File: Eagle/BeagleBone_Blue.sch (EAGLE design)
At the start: 166 parts, among them M1 JST_ZH_2, M2 JST_ZH_2, M3 JST_ZH_2, M4 JST_ZH_2, Q3 MOSFET-N, U1 OSD3358, U2 CM200C-32.768KAZF-UT, U3 DMC564040R, U4 DMC564040R, U5 24LC_32AT-I/OT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

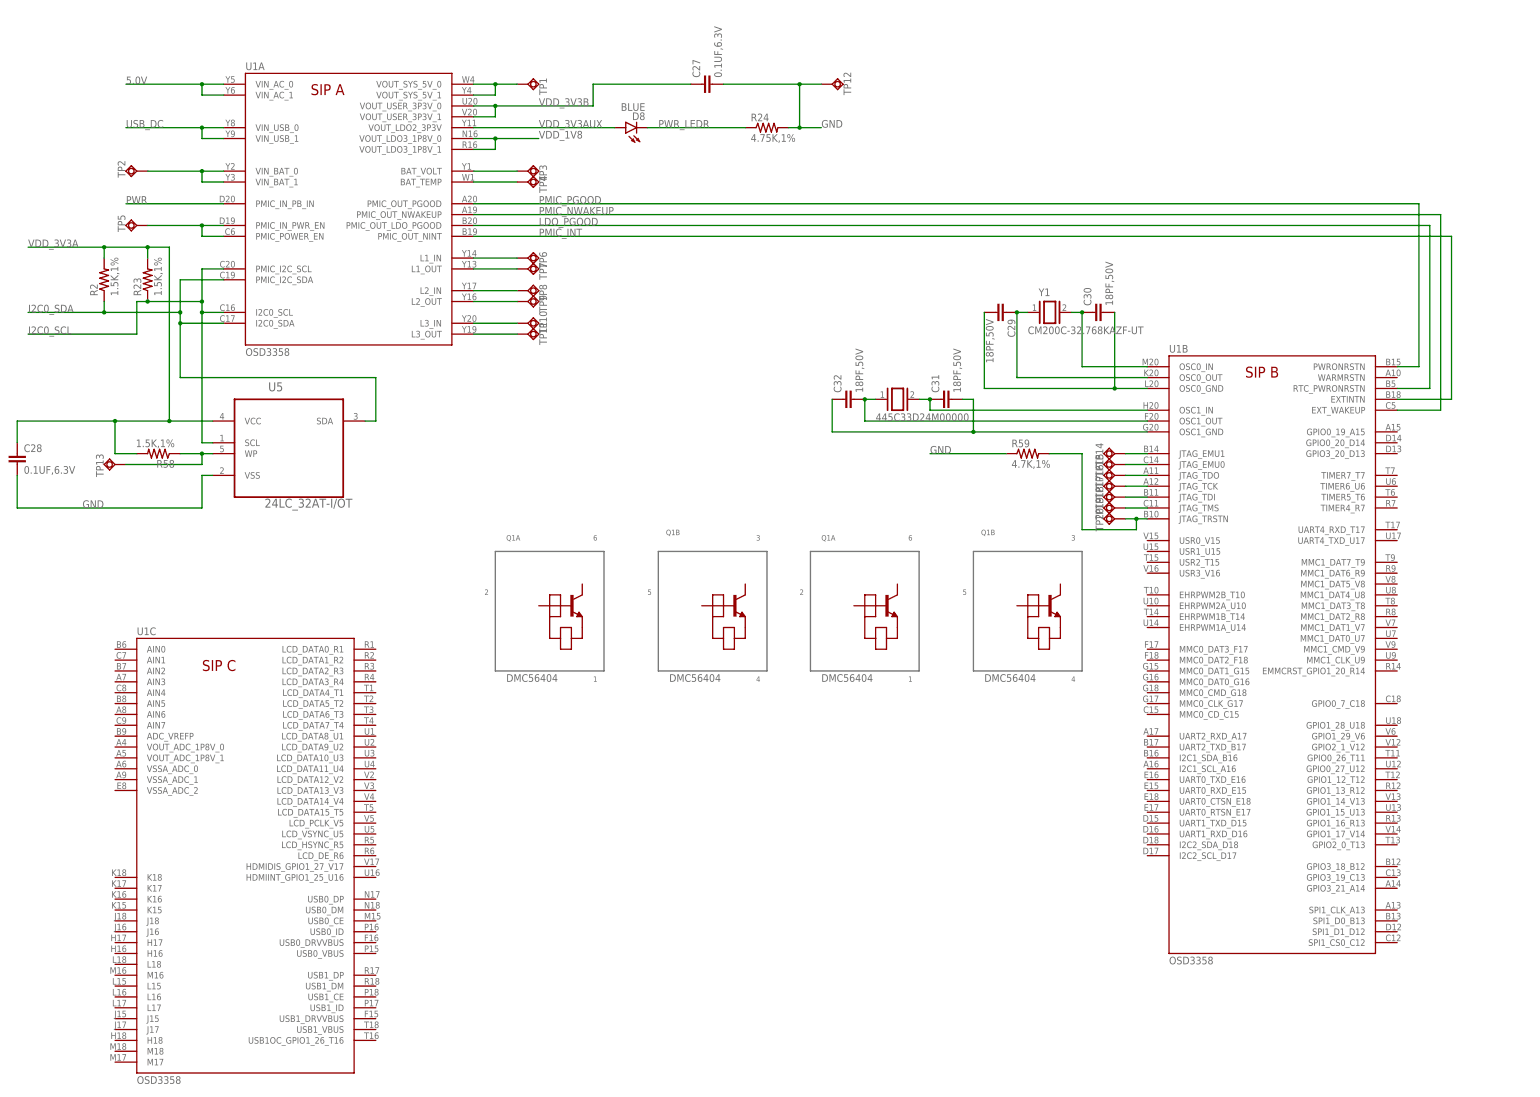
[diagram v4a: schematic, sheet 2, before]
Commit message: Added USRx LEDs
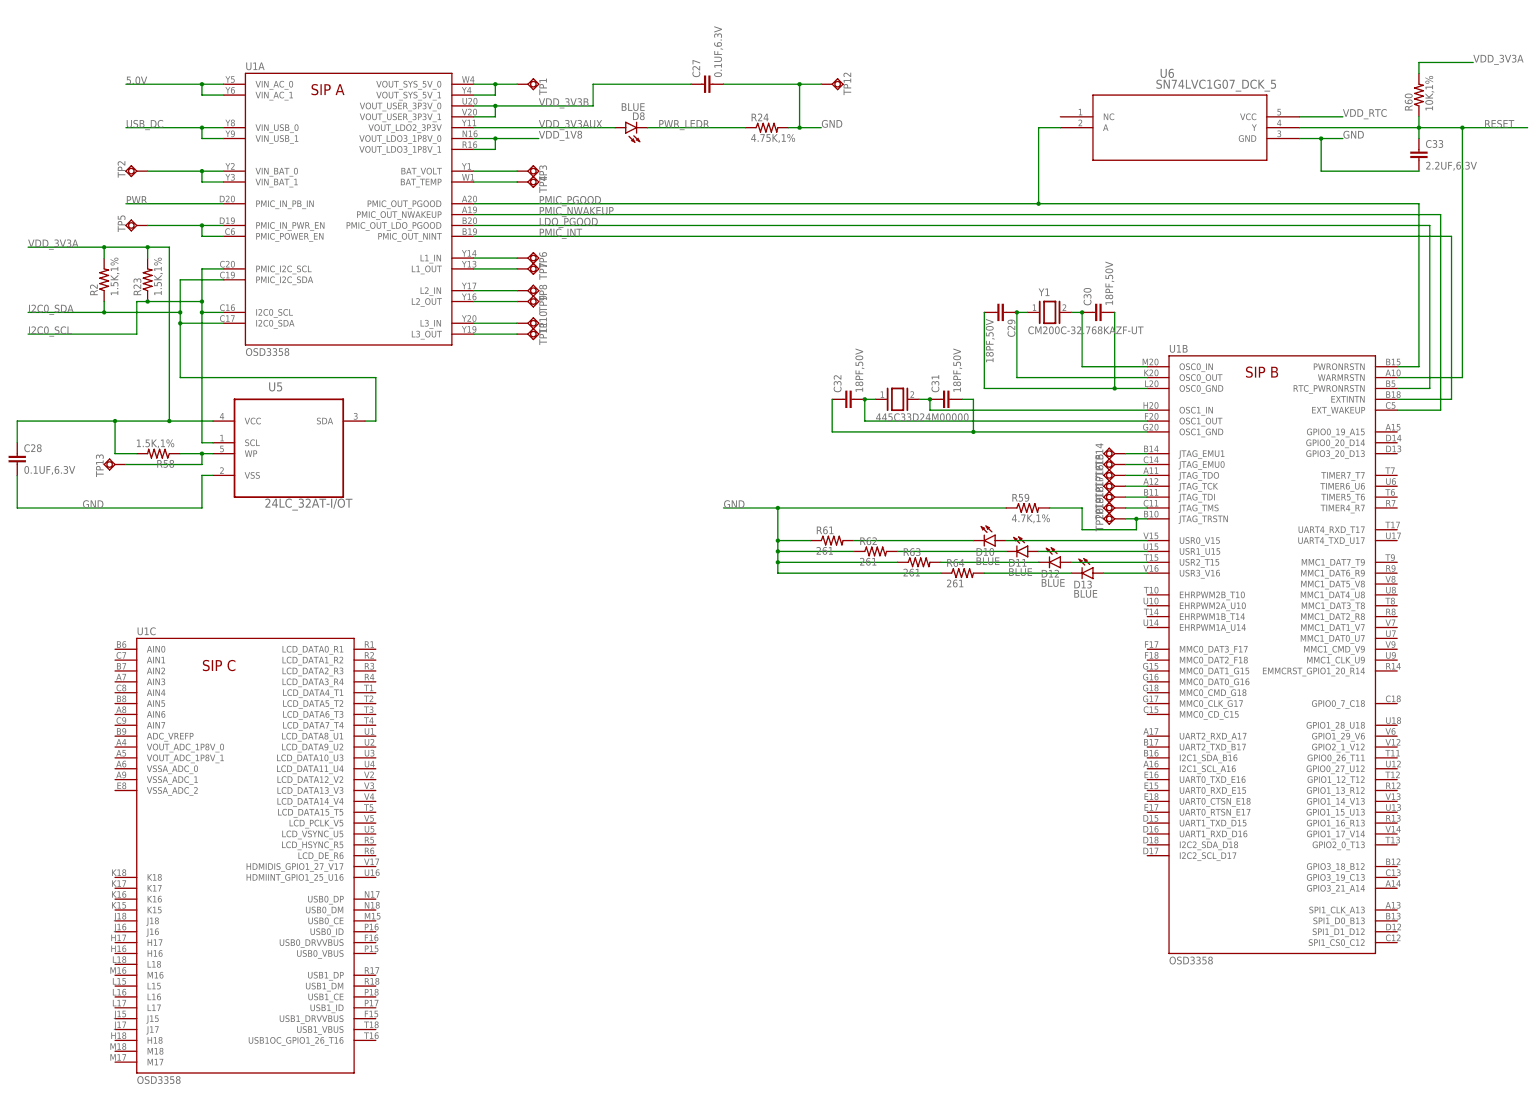
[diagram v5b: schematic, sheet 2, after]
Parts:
- removed U3, U4: DMC564040R, DMC564040R:DMC564040R
- added C33: 2.2UF,6.3V, Strawson_Eagle_Lib:CAP0402-CAP
- added D10, D11, D12, D13: BLUE, BeagleBone_Blue:LED0603
- added R60: 10K,1%, Strawson_Eagle_Lib:RESISTOR0402-RES
- added R61, R62, R63, R64: 261, Strawson_Eagle_Lib:RESISTOR0402-RES
- added U6: SN74LVC1G07_DCK_5, SN74LVC1G07:SN74LVC1G07_DCK_5
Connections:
- new net N$43: D13.A, U1B.USR3_V16
- new net N$44: D12.A, U1B.USR2_T15
- new net N$45: D11.A, U1B.USR1_U15
- new net N$46: D10.A, U1B.USR0_V15
- new net N$47: D10.C, R61.2
- new net N$57: D11.C, R62.2
- new net N$58: D12.C, R63.2
- new net N$59: D13.C, R64.2
- new net VDD_RTC: U6.VCC
- net GND: now also C33.2, R61.1, R62.1, R63.1, R64.1, U6.GND
- net PMIC_PGOOD: now also U6.A
- net RESET: now also C33.1, R60.1, U1B.WARMRSTN, U6.Y
- net VDD_3V3A: now also R60.2
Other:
- moved on the sheet: R59
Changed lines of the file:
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@@
 <part name="C27" library="Strawson_Eagle_Lib" deviceset="CAP" device="0402-CAP" value="0.1UF,6.3V"/>
 <part name="U2" library="CM200C-32.768KAZF-UT" deviceset="CM200C-32.768KAZF-UT" device=""/>
-<part name="U3" library="DMC564040R" deviceset="DMC564040R" device=""/>
-<part name="U4" library="DMC564040R" deviceset="DMC564040R" device=""/>
 <part name="U5" library="Microchip-24LCxxx" deviceset="24LC_" device="" technology="32AT-I/OT"/>
 <part name="R58" library="Strawson_Eagle_Lib" deviceset="RESISTOR" device="0402-RES" value="1.5K,1%"/>
@@
 <part name="TP20" library="testpad" deviceset="TPSQ" device="B1,27"/>
 <part name="R59" library="Strawson_Eagle_Lib" deviceset="RESISTOR" device="0402-RES" value="4.7K,1%"/>
+<part name="U6" library="SN74LVC1G07" deviceset="SN74LVC1G07_DCK_5" device=""/>
+<part name="C33" library="Strawson_Eagle_Lib" deviceset="CAP" device="0402-CAP" value="2.2UF,6.3V"/>
+<part name="R60" library="Strawson_Eagle_Lib" deviceset="RESISTOR" device="0402-RES" value="10K,1%"/>
+<part name="D10" library="BeagleBone_Blue" deviceset="LED" device="0603" value="BLUE"/>
+<part name="D11" library="BeagleBone_Blue" deviceset="LED" device="0603" value="BLUE"/>
+<part name="D12" library="BeagleBone_Blue" deviceset="LED" device="0603" value="BLUE"/>
+<part name="D13" library="BeagleBone_Blue" deviceset="LED" device="0603" value="BLUE"/>
+<part name="R61" library="Strawson_Eagle_Lib" deviceset="RESISTOR" device="0402-RES" value="261"/>
+<part name="R62" library="Strawson_Eagle_Lib" deviceset="RESISTOR" device="0402-RES" value="261"/>
+<part name="R63" library="Strawson_Eagle_Lib" deviceset="RESISTOR" device="0402-RES" value="261"/>
+<part name="R64" library="Strawson_Eagle_Lib" deviceset="RESISTOR" device="0402-RES" value="261"/>
 </parts>
 <sheets>
@@
 <instance part="C27" gate="G$1" x="180.34" y="248.92" rot="R90"/>
 <instance part="U2" gate="G$1" x="307.34" y="182.88"/>
-<instance part="U3" gate="G$1" x="238.76" y="121.92"/>
-<instance part="U4" gate="G$1" x="165.1" y="121.92"/>
 <instance part="U5" gate="A" x="63.5" y="170.18"/>
 <instance part="R58" gate="G$1" x="50.8" y="162.56" rot="R180"/>
@@
 <instance part="TP19" gate="G$1" x="274.32" y="149.86" rot="R270"/>
 <instance part="TP20" gate="G$1" x="274.32" y="147.32" rot="R270"/>
-<instance part="R59" gate="G$1" x="254" y="162.56"/>
+<instance part="R59" gate="G$1" x="254" y="149.86"/>
+<instance part="U6" gate="A" x="261.62" y="241.3"/>
+<instance part="C33" gate="G$1" x="345.44" y="231.14"/>
+<instance part="R60" gate="G$1" x="345.44" y="246.38" rot="R90"/>
+<instance part="D10" gate="G$1" x="246.38" y="142.24" rot="R270"/>
+<instance part="D11" gate="G$1" x="254" y="139.7" rot="R270"/>
+<instance part="D12" gate="G$1" x="261.62" y="137.16" rot="R270"/>
+<instance part="D13" gate="G$1" x="269.24" y="134.62" rot="R270"/>
+<instance part="R61" gate="G$1" x="208.28" y="142.24"/>
+<instance part="R62" gate="G$1" x="218.44" y="139.7"/>
+<instance part="R63" gate="G$1" x="228.6" y="137.16"/>
+<instance part="R64" gate="G$1" x="238.76" y="134.62"/>
 </instances>
 <busses>
@@
 <junction x="40.64" y="170.18"/>
 </segment>
+<segment>
+<pinref part="R60" gate="G$1" pin="2"/>
+<wire x1="345.44" y1="251.46" x2="345.44" y2="254" width="0.1524" layer="91"/>
+<wire x1="345.44" y1="254" x2="358.14" y2="254" width="0.1524" layer="91"/>
+<label x="358.14" y="254" size="1.778" layer="95"/>
+</segment>
 </net>
 <net name="VDD_3V3B" class="0">
@@
 <segment>
 <pinref part="R59" gate="G$1" pin="1"/>
-<wire x1="248.92" y1="162.56" x2="231.14" y2="162.56" width="0.1524" layer="91"/>
-<label x="231.14" y="162.56" size="1.778" layer="95"/>
+<wire x1="248.92" y1="149.86" x2="195.58" y2="149.86" width="0.1524" layer="91"/>
+<label x="182.88" y="149.86" size="1.778" layer="95"/>
+<pinref part="R64" gate="G$1" pin="1"/>
+<wire x1="195.58" y1="149.86" x2="182.88" y2="149.86" width="0.1524" layer="91"/>
+<wire x1="233.68" y1="134.62" x2="195.58" y2="134.62" width="0.1524" layer="91"/>
+<wire x1="195.58" y1="134.62" x2="195.58" y2="137.16" width="0.1524" layer="91"/>
+<junction x="195.58" y="149.86"/>
+<pinref part="R63" gate="G$1" pin="1"/>
+<wire x1="195.58" y1="137.16" x2="195.58" y2="139.7" width="0.1524" layer="91"/>
+<wire x1="195.58" y1="139.7" x2="195.58" y2="142.24" width="0.1524" layer="91"/>
+<wire x1="195.58" y1="142.24" x2="195.58" y2="149.86" width="0.1524" layer="91"/>
+<wire x1="223.52" y1="137.16" x2="195.58" y2="137.16" width="0.1524" layer="91"/>
+<junction x="195.58" y="137.16"/>
+<pinref part="R62" gate="G$1" pin="1"/>
+<wire x1="213.36" y1="139.7" x2="195.58" y2="139.7" width="0.1524" layer="91"/>
+<junction x="195.58" y="139.7"/>
+<pinref part="R61" gate="G$1" pin="1"/>
+<wire x1="203.2" y1="142.24" x2="195.58" y2="142.24" width="0.1524" layer="91"/>
+<junction x="195.58" y="142.24"/>
+</segment>
+<segment>
+<pinref part="U6" gate="A" pin="GND"/>
+<wire x1="327.66" y1="236.22" x2="322.58" y2="236.22" width="0.1524" layer="91"/>
+<label x="327.66" y="236.22" size="1.778" layer="95"/>
+<wire x1="322.58" y1="236.22" x2="317.5" y2="236.22" width="0.1524" layer="91"/>
+<wire x1="322.58" y1="236.22" x2="322.58" y2="228.6" width="0.1524" layer="91"/>
+<junction x="322.58" y="236.22"/>
+<pinref part="C33" gate="G$1" pin="2"/>
+<wire x1="322.58" y1="228.6" x2="345.44" y2="228.6" width="0.1524" layer="91"/>
 </segment>
 </net>
@@
 <pinref part="U1" gate="A" pin="PMIC_OUT_PGOOD"/>
 <label x="139.7" y="220.98" size="1.778" layer="95"/>
-<wire x1="124.46" y1="220.98" x2="345.44" y2="220.98" width="0.1524" layer="91"/>
+<wire x1="124.46" y1="220.98" x2="256.54" y2="220.98" width="0.1524" layer="91"/>
+<wire x1="256.54" y1="220.98" x2="345.44" y2="220.98" width="0.1524" layer="91"/>
 <wire x1="345.44" y1="220.98" x2="345.44" y2="182.88" width="0.1524" layer="91"/>
 <pinref part="U1" gate="B" pin="PWRONRSTN"/>
 <wire x1="345.44" y1="182.88" x2="340.36" y2="182.88" width="0.1524" layer="91"/>
+<wire x1="256.54" y1="220.98" x2="256.54" y2="238.76" width="0.1524" layer="91"/>
+<junction x="256.54" y="220.98"/>
+<pinref part="U6" gate="A" pin="A"/>
+<wire x1="256.54" y1="238.76" x2="261.62" y2="238.76" width="0.1524" layer="91"/>
 </segment>
 </net>
@@
 <pinref part="R59" gate="G$1" pin="2"/>
 <wire x1="279.4" y1="147.32" x2="281.94" y2="147.32" width="0.1524" layer="91"/>
-<wire x1="259.08" y1="162.56" x2="266.7" y2="162.56" width="0.1524" layer="91"/>
-<wire x1="266.7" y1="162.56" x2="266.7" y2="144.78" width="0.1524" layer="91"/>
+<wire x1="259.08" y1="149.86" x2="266.7" y2="149.86" width="0.1524" layer="91"/>
+<wire x1="266.7" y1="149.86" x2="266.7" y2="144.78" width="0.1524" layer="91"/>
 <wire x1="266.7" y1="144.78" x2="279.4" y2="144.78" width="0.1524" layer="91"/>
 <wire x1="279.4" y1="144.78" x2="279.4" y2="147.32" width="0.1524" layer="91"/>
@@
 </segment>
 </net>
+<net name="RESET" class="0">
+<segment>
+<pinref part="U6" gate="A" pin="Y"/>
+<wire x1="317.5" y1="238.76" x2="345.44" y2="238.76" width="0.1524" layer="91"/>
+<wire x1="345.44" y1="238.76" x2="355.6" y2="238.76" width="0.1524" layer="91"/>
+<wire x1="355.6" y1="238.76" x2="355.6" y2="180.34" width="0.1524" layer="91"/>
+<pinref part="U1" gate="B" pin="WARMRSTN"/>
+<wire x1="355.6" y1="180.34" x2="340.36" y2="180.34" width="0.1524" layer="91"/>
+<wire x1="355.6" y1="238.76" x2="370.84" y2="238.76" width="0.1524" layer="91"/>
+<junction x="355.6" y="238.76"/>
+<label x="360.68" y="238.76" size="1.778" layer="95"/>
+<pinref part="C33" gate="G$1" pin="1"/>
+<wire x1="345.44" y1="236.22" x2="345.44" y2="238.76" width="0.1524" layer="91"/>
+<junction x="345.44" y="238.76"/>
+<pinref part="R60" gate="G$1" pin="1"/>
+<wire x1="345.44" y1="238.76" x2="345.44" y2="241.3" width="0.1524" layer="91"/>
+</segment>
+</net>
+<net name="VDD_RTC" class="0">
+<segment>
+<pinref part="U6" gate="A" pin="VCC"/>
+<wire x1="317.5" y1="241.3" x2="327.66" y2="241.3" width="0.1524" layer="91"/>
+<label x="327.66" y="241.3" size="1.778" layer="95"/>
+</segment>
+</net>
+<net name="N$43" class="0">
+<segment>
+<pinref part="U1" gate="B" pin="USR3_V16"/>
+<pinref part="D13" gate="G$1" pin="A"/>
+<wire x1="281.94" y1="134.62" x2="271.78" y2="134.62" width="0.1524" layer="91"/>
+</segment>
+</net>
+<net name="N$44" class="0">
+<segment>
+<pinref part="U1" gate="B" pin="USR2_T15"/>
+<pinref part="D12" gate="G$1" pin="A"/>
+<wire x1="281.94" y1="137.16" x2="264.16" y2="137.16" width="0.1524" layer="91"/>
+</segment>
+</net>
+<net name="N$45" class="0">
+<segment>
+<pinref part="U1" gate="B" pin="USR1_U15"/>
+<pinref part="D11" gate="G$1" pin="A"/>
+<wire x1="281.94" y1="139.7" x2="256.54" y2="139.7" width="0.1524" layer="91"/>
+</segment>
+</net>
+<net name="N$46" class="0">
+<segment>
+<pinref part="U1" gate="B" pin="USR0_V15"/>
+<pinref part="D10" gate="G$1" pin="A"/>
+<wire x1="281.94" y1="142.24" x2="248.92" y2="142.24" width="0.1524" layer="91"/>
+</segment>
+</net>
+<net name="N$47" class="0">
+<segment>
+<pinref part="D10" gate="G$1" pin="C"/>
+<pinref part="R61" gate="G$1" pin="2"/>
+<wire x1="241.3" y1="142.24" x2="213.36" y2="142.24" width="0.1524" layer="91"/>
+</segment>
+</net>
+<net name="N$57" class="0">
+<segment>
+<pinref part="D11" gate="G$1" pin="C"/>
+<pinref part="R62" gate="G$1" pin="2"/>
+<wire x1="248.92" y1="139.7" x2="223.52" y2="139.7" width="0.1524" layer="91"/>
+</segment>
+</net>
+<net name="N$58" class="0">
+<segment>
+<pinref part="D12" gate="G$1" pin="C"/>
+<pinref part="R63" gate="G$1" pin="2"/>
+<wire x1="256.54" y1="137.16" x2="233.68" y2="137.16" width="0.1524" layer="91"/>
+</segment>
+</net>
+<net name="N$59" class="0">
+<segment>
+<pinref part="D13" gate="G$1" pin="C"/>
+<pinref part="R64" gate="G$1" pin="2"/>
+<wire x1="264.16" y1="134.62" x2="243.84" y2="134.62" width="0.1524" layer="91"/>
+</segment>
+</net>
